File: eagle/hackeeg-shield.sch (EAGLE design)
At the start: 142 parts, among them IC1 ADS1299IPAG, IC10 TXB0108PWR, IC11 TXB0108PWR, IC2 TPS72325DBVT, IC3 TPS73225DBVT, IC5 24AA256UID, IC6 TPS60403DBVT, IC7 OPA376DBV, IC8 OPA376DBV, IC9 TXS0102DCUR

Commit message: Modified version that uses isolated SPI and isolated DC-DC converter (not tested much!)
To enable use of the EMG shield while the Arduino is galvanically connected to mains (in our scenario since it also containers motor driver controllers).

Basic communication works, but signal quality is not tested yet.

Issues:
- Spikes in signals, probably SPI issues
- MCU led polarity is wrong
- AIMTEC isolator doesn't fit well (keep out area is on the wrong side)
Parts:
- removed C43, C45, C47, C49: 4.7nF, SparkFun-Passives:CAP0603-CAP
- removed C51, C52, C54, C56, C58, C61, C70, C72: 1uF, SparkFun-Passives:CAP0603-CAP
- removed C53, C55, C57, C59, C71, C73: 0.1uF, SparkFun-Passives:CAP0603-CAP
- removed C66: 0.01uF, SparkFun-Passives:CAP0603-CAP
- removed IC10, IC11: TXB0108PWR, adafruit:TXB0108PWR
- removed IC2: TPS72325DBVT, TPS723xx:TPS732XXDBV
- removed IC3: TPS73225DBVT, TPS32xx:TPS732XXDBV
- removed IC5: 24AA256UID, microchip:24LC256SN
- removed IC6: TPS60403DBVT, TPS604xx:TPS604XXDBV
- removed IC9: TXS0102DCUR, adafruit:TXS0102
- removed JP1: CONFIG1, headers:PINHD-2X12
- removed JP15: External Sync, SparkFun-Connectors:M04JST-PTH
- removed JP16: Electrodes, OS302-R241:302-R241
- removed JP2: CONFIG0, headers:PINHD-2X10
- removed JP23: XIO, SmartPrj:PINHD-2X18
- removed JP3: BOARD_ADDRESS, headers:PINHD-2X4
- removed JP4: 5V-2.5V, headers:PINHD-1X3
- removed JP5: -2.5V-GND, headers:PINHD-1X3
- removed JP6: SRB1-BIAS, adafruit:PINHD-1X3
- removed JP7: SRB2-REF_ELEC, adafruit:PINHD-1X3
- removed JP8: SRB1-REF_ELEC, adafruit:PINHD-1X3
- removed JP9: BIASOUT_BIASIN_BIAS_ELEC, headers:PINHD-1X3
- removed R19, R20, R21: 10k, SparkFun-Passives:RESISTOR0603-RES
- removed R24: 4.99k, SparkFun-Passives:RESISTOR0603-RES
- removed SPI: SPI, SmartPrj:PINHD-2X3
- removed TP2: AVSS_TEST_POINT, adafruit:PINHD-1X1
- added C67, C69: 0.1uF, SparkFun-Passives:CAP0603-CAP
- added D3, D4: BLUE, SparkFun-LED:LED-WHITE
- added ESD1, ESD2, ESD3, ESD4, ESD5, ESD6, ESD7, ESD8: ESD7L, ESD7L:ESD7L
- added ISO1: AM1DM-0505SH60-NZ, Aimtec AM1D:AM1DM-0505SH60-NZ
- added J1, J10, J11: 533981071, Molex Picoblade 53398-1071:533981071
- added J2, J3, J4, J5, J6, J7, J8, J9: SJ1-3535N, SJ1-3535N-a:SJ1-3535N
- added R10, R11: 4.99k, SparkFun-Passives:RESISTOR0603-RES
- added R12, R13, R14, R15, R16, R17: 0R, SparkFun-Passives:RESISTOR0603-RES
- added R5, R8: 270, SparkFun-Passives:RESISTOR0603-RES
- added R7: 1k, SparkFun-Passives:RESISTOR0603-RES
- added R9: 10k, SparkFun-Passives:RESISTOR0603-RES
- added SJ4: CLK_SEL, jumper:SJ2W
- added SW1: SPST_TACT-EVQQ2, adafruit:SPST_TACT-EVQQ2
- added U1: R1SE-0505-R, R1SE-0505-R:R1SE-0505-R
- added U2: MAX14483AAP+, MAX14483AAP:MAX14483AAP+
- added U3, U4: ADP151AUJZ-3.3, ADP151AUJZ-3.3:ADP151AUJZ-3.3
- C1, C28: value 2.2uF -> 10uF
- C2: value 10 uF -> 4.7uF
- C26: value 1uF -> 10pF
- C29, C30: value 1uF -> 100nF
- C3: value 10uF -> 4.7uF
- C31: value 0.01uF -> 10pF
- C32: value 1uF -> 100pF
- C34, C36, C38, C40, C42, C44, C46, C48, C62: value 4.7nF -> NC
- C35: value 4.7nF -> 1 pF TVS
- C37: value 4.7nF -> 220pF
- C39, C41: value 4.7nF -> 100nF
- C4: value 2.2uF -> 1uF
- D1: value RED -> GREEN
- D2: value BLUE -> ORANGE
- L1: value 3.3 uH -> 6.8μH; device SparkFun-Passives:INDUCTOR0805 -> SparkFun-Coils:1.0μH-0805_WIDE-1.0μH-1.4A-0.07OHM-1.4MM_H; SPICEPREFIX (none) -> L
- L2, L3, L4: value 3.3 uH -> 3.3μH; device SparkFun-Passives:INDUCTOR0805 -> SparkFun-Coils:1.0μH-0805_WIDE-1.0μH-1.4A-0.07OHM-1.4MM_H
- R6: value 3.98K -> 4.99k
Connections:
- removed net !ADC_CS_0: JP2.10, JP21.4
- removed net !ADC_CS_1: JP2.12, JP20.8
- removed net !ADC_CS_2: JP2.14, JP23.33
- removed net !ADC_CS_3: JP2.16, JP23.4
- removed net !ADC_PWDN_0: JP1.22, JP23.13
- removed net !ADC_PWDN_1: JP1.24, JP23.14
- removed net !ADC_RESET_0: JP1.18, JP23.27
- removed net !ADC_RESET_1: JP1.20, JP23.28
- removed net !ADS_PWDN: IC11.B5, JP1.21, JP1.23
- removed net !ADS_RESET: IC11.B1, JP1.17, JP1.19
- removed net !ADS_SPI_CS: IC11.B6, JP2.11, JP2.13, JP2.15, JP2.9
- removed net +2.5V: C6.1, JP4.3, L2.2
- removed net -2.5V: C3.1, JP5.1, L1.2
- removed net ADC_CLK_0: JP1.10, JP25.8
- removed net ADC_CLK_1: JP1.12, JP25.5
- removed net ADC_DRDY_0: JP1.2, JP23.5
- removed net ADC_DRDY_1: JP1.4, JP23.6
- removed net ADC_DRDY_2: JP1.6, JP23.7
- removed net ADC_DRDY_3: JP1.8, JP23.8
- removed net ADC_START_0: JP1.14, JP23.11
- removed net ADC_START_1: JP1.16, JP23.12
- removed net ADS_CLK: IC10.B5, JP1.11, JP1.9
- removed net ADS_CLKSEL: IC10.B1, JP23.29
- removed net ADS_DRDY: IC10.B2, JP1.1, JP1.3, JP1.5, JP1.7
- removed net ADS_SPI_CLK: IC10.B4, JP15.3, JP2.5, JP2.7
- removed net ADS_SPI_IN: IC10.B6, JP2.17, JP2.19
- removed net ADS_SPI_OUT: IC10.B3, JP2.1, JP2.3
- removed net ADS_START: IC11.B2, JP1.13, JP1.15, JP15.2
- removed net ARD_SCL: IC9.B2, JP22.8
- removed net ARD_SDA: IC9.B1, JP22.7
- removed net AVSS: C11.2, C12.2, C17.2, C18.2, C19.2, C20.2, C21.2, C22.2, C23.2, C29.2, C30.2, C33.2, C51.2, C61.2, C7.2, C8.2, IC1.AVSS1, IC1.AVSS@1, IC1.AVSS@2, IC1.AVSS@3, IC1.AVSS@4, IC1.AVSS@5, IC1.VREFN, IC7.V_N, IC8.V_N, JP5.2, R22.2, TP2.1
- removed net BIASIN: IC1.BIASIN, JP9.3
- removed net BIASOUT: C66.1, IC1.BIASOUT, JP9.2, R6.2
- removed net BIAS_ELEC: JP6.1, JP9.1, R24.2
- removed net BIAS_ELEC_CON: JP16.24, R24.1
- removed net IOREF: C54.2, C55.2, C58.2, C59.2, C72.2, C73.2, IC10.VCCB, IC11.VCCB, IC9.VCCB, JP26.2
- removed net N$101: JP23.15
- removed net N$102: JP23.17
- removed net N$103: JP23.19
- removed net N$104: JP23.21
- removed net N$107: JP23.23
- removed net N$108: JP23.25
- removed net N$111: JP23.31
- removed net N$24: JP21.7
- removed net N$27: JP20.3
- removed net N$28: JP20.4
- removed net N$29: JP20.5
- removed net N$30: JP20.6
- removed net N$31: JP20.7
- removed net N$33: JP20.10
- removed net N$34: JP21.1
- removed net N$35: JP21.2
- removed net N$36: JP21.3
- removed net N$37: IC9.OE, R4.2
- removed net N$38: JP21.5
- removed net N$39: JP21.6
- removed net N$40: JP21.8
- removed net N$41: JP22.1
- removed net N$42: JP22.2
- removed net N$45: JP22.5
- removed net N$46: JP22.6
- removed net N$48: JP24.8
- removed net N$49: JP24.7
- removed net N$50: JP24.6
- removed net N$501: JP25.7
- removed net N$51: JP24.5
- removed net N$510: JP25.6
- removed net N$52: JP24.4
- removed net N$53: JP24.3
- removed net N$561: IC10.OE, R2.2
- removed net N$562: IC11.OE, R3.2
- removed net N$570: JP26.5
- removed net N$571: JP23.1
- removed net N$572: JP23.2
- removed net N$59: JP25.4
- removed net N$60: JP25.3
- removed net N$6001: JP20.2
- removed net N$6002: JP20.1
- removed net N$61: JP25.2
- removed net N$62: JP26.8
- removed net N$63: JP26.7
- removed net N$64: JP26.6
- removed net N$67: JP26.3
- removed net N$78: JP23.34
- removed net N$79: JP23.32
- removed net N$80: JP23.30
- removed net N$82: JP23.26
- removed net N$83: JP23.24
- removed net N$84: JP23.22
- removed net N$85: JP23.20
- removed net N$86: JP23.18
- removed net N$87: JP23.16
- removed net N$90: JP23.10
- removed net N$95: JP23.3
- removed net N$98: JP23.9
- removed net RESET: SPI.5
- removed net SCL: IC5.SCL, IC9.A2
- removed net SDA: IC5.SDA, IC9.A1
- removed net SPI0_MISO: JP2.2, SPI.1
- removed net SPI0_MOSI: JP2.18, SPI.4
- removed net SPI0_SCK: JP2.8, SPI.3
- removed net USART1_MISO: JP2.4, JP22.4
- removed net USART1_MOSI: JP2.20, JP22.3
- removed net USART1_SCK: JP2.6, JP25.1
- removed net VCC_-5V: C24.1, C28.1, IC2.EN, IC2.IN, L3.2
- new net DRDY_D69: JP24.1, R17.1
- new net N$12: R17.2, U2.!OFAULT
- new net N$22: R15.2, U2.IAUX
- new net N$23: R16.2, U2.OSDO
- new net N$44: R7.2, U2.!SDOEN
- new net PE: C2.2, C3.2, C67.2, ISO1.VIN-, JP26.6, JP26.7, R7.1, R8.1, U1.-VIN, U2.GNDB
- new net PGND: C26.1, C31.1, C32.2, IC1.BIASIN, J10.10, J2.1, R10.2, R11.2
- new net SPI2_CS: JP20.2, R12.1
- new net SPI2_MISO: JP25.5, R16.1
- new net SPI2_MOSI: JP25.3, R14.1
- new net SPI2_SCK: JP22.7, R13.1
- new net START_D68: JP24.2, R15.1
- new net VCC_MCU: C2.1, C67.1, JP26.5, L1.1, U2.VDDB
- net !PWDN: now also C41.1, R4.1, SW1.P, SW1.P1; no longer IC11.A5
- net !RESET: now also C39.1, R9.1; no longer IC11.A1
- net !SPI_CS: now also J1.4, R2.2, U2.!OCS; no longer IC11.A6
- net AGND: now also C11.2, C12.2, C17.2, C18.2, C19.2, C20.2, C21.2, C22.2, C23.2, C29.2, C32.1, C33.2, C35.2, C69.2, C7.2, C8.2, D3.C, ESD1.P$3, ESD2.P$3, ESD3.P$3, ESD4.P$3, ESD5.P$3, ESD6.P$3, ESD7.P$3, ESD8.P$3, IC1.AVSS1, IC1.AVSS@1, IC1.AVSS@2, IC1.AVSS@3, IC1.AVSS@4, IC1.AVSS@5, IC1.VREFN, IC7.V_N, IC8.V_N, ISO1.VOUT-, J1.1, J1.11, J1.12, J10.11, J10.12, J11.11, J11.12, R22.2, SJ4.3, SW1.S, SW1.S1, U1.-VOUT, U2.!IRDY, U2.GNDA, U3.GND, U4.GND; no longer C2.2, C29.1, C3.2, C31.2, C32.2, C34.2, C35.1, C36.2, C37.1, C38.2, C39.1, C40.2, C41.1, C42.2, C43.1, C44.2, C45.1, C46.2, C47.1, C48.2, C49.1, C51.1, C52.1, C53.1, C54.1, C55.1, C56.1, C57.1, C58.1, C59.1, C61.1, C70.1, C71.1, C72.1, C73.1, IC10.A7, IC10.A8, IC10.B7, IC10.B8, IC10.GND, IC11.A3, IC11.A4, IC11.A7, IC11.A8, IC11.B3, IC11.B4, IC11.B7, IC11.B8, IC11.GND, IC2.GND, IC3.GND, IC5.GND, IC5.WP, IC6.GND, IC9.GND, JP15.4, JP16.4, JP16.5, JP16.6, JP23.35, JP23.36, JP5.3, R19.1, R20.1, R21.1, SPI.6
- net AIN1N: now also C34.2; no longer C35.2
- net AIN2N: now also C36.2; no longer C37.2
- net AIN3N: now also C38.2; no longer C39.2
- net AIN4N: now also C40.2; no longer C41.2
- net AIN5N: now also C42.2; no longer C43.2
- net AIN6N: now also C44.2; no longer C45.2
- net AIN7N: now also C46.2; no longer C47.2
- net AIN8N: now also C48.2; no longer C49.2
- net AVDD: now also C29.1, C30.2, C6.1, L2.2; no longer JP16.2, JP4.2
- net BIASINV: now also R6.2; no longer C66.2, JP15.1, JP16.3, R6.1
- net BOARD_ADDR_0: no longer IC5.A0, JP3.3, R19.2
- net BOARD_ADDR_1: no longer IC5.A1, JP3.1, R20.2
- net BOARD_ADDR_2: no longer IC5.A2, R21.2
- net CLK: now also J1.3; no longer IC10.A5
- net CLKSEL: now also R3.1; no longer IC10.A1
- net DRDY: now also J1.9, U2.!IFAULT; no longer IC10.A2
- net DVDD: now also C24.1, C39.2, C41.2, C69.1, L3.2, R4.2, R9.2, SJ4.1, U2.VDDA; no longer C52.2, C53.2, C56.2, C57.2, C70.2, C71.2, IC10.VCCA, IC11.VCCA, IC5.VCC, IC9.VCCA, JP16.1, JP26.4, JP3.2, JP3.4, R3.1, R4.1
- net IN1N: now also ESD1.P$2, J10.7, J2.3; no longer JP16.8
- net IN1P: now also ESD1.P$1, J10.8, J2.2; no longer JP16.7
- net IN2N: now also ESD2.P$2, J10.5, J3.3; no longer JP16.10
- net IN2P: now also ESD2.P$1, J10.6, J3.2; no longer JP16.9
- net IN3N: now also ESD3.P$2, J10.3, J4.3; no longer JP16.12
- net IN3P: now also ESD3.P$1, J10.4, J4.2; no longer JP16.11
- net IN4N: now also ESD4.P$2, J10.1, J5.3; no longer JP16.14
- net IN4P: now also ESD4.P$1, J10.2, J5.2; no longer JP16.13
- net IN5N: now also ESD5.P$2, J11.9, J6.3; no longer JP16.16
- net IN5P: now also ESD5.P$1, J11.10, J6.2; no longer JP16.15
- net IN6N: now also ESD6.P$2, J11.7, J7.3; no longer JP16.18
- net IN6P: now also ESD6.P$1, J11.8, J7.2; no longer JP16.17
- net IN7N: now also ESD7.P$2, J11.5, J8.3; no longer JP16.20
- net IN7P: now also ESD7.P$1, J11.6, J8.2; no longer JP16.19
- net IN8N: now also ESD8.P$2, J11.3, J9.3; no longer JP16.22
- net IN8P: now also ESD8.P$1, J11.4, J9.2; no longer JP16.21
- net N$1: now also U4.VOUT; no longer IC3.OUT
- net N$10: now also J11.1, R6.1; no longer C26.1, IC6.CFLY_N
- net N$11: now also R5.1, U2.SBA; no longer C32.1, IC3.NR/FB
- net N$13: now also D4.C, U2.SAA; no longer C31.1, IC2.NR/FB
- net N$16: now also R12.2, U2.!ICS; no longer IC8.P_IN, JP7.2
- net N$17: now also R13.2, U2.ISCLK; no longer IC8.N_IN, IC8.OUT, JP8.3
- net N$18: now also C31.2, C37.1, R10.1; no longer IC7.N_IN, JP6.3
- net N$2: now also C15.1, C16.1, L3.1, U3.VOUT; no longer C1.1, C2.1, IC2.OUT, L1.1
- net N$20: now also R3.2, SJ4.2; no longer JP24.1
- net N$21: now also R14.2, U2.ISDI; no longer JP26.1
- net N$54: now also C26.2, C37.2, IC7.N_IN, R11.1; no longer JP24.2
- net N$6: now also C3.1, ISO1.VIN+, L1.2, U1.+VIN; no longer JP20.9
- net N$7: now also D4.A, R8.2; no longer C15.1, C16.1, IC6.OUT, L3.1
- net N$9: now also D3.A, R5.2; no longer C26.2, IC6.CFLY_P
- net REF_ELEC: now also IC8.P_IN; no longer JP7.1, JP8.1
- net REF_ELEC_CON: now also C35.1, J10.9, J3.1; no longer JP16.23
- net SPI_CLK: now also J1.5, U2.OSCLK; no longer IC10.A4
- net SPI_IN: now also J1.6, U2.OSDI; no longer IC10.A6
- net SPI_OUT: now also J1.8, U2.ISDO; no longer IC10.A3
- net SRB1: now also IC1.SRB1, IC8.N_IN, IC8.OUT; no longer IC1.SRB2, JP6.2, JP8.2
- net SRB2: now also IC1.SRB2, J1.10; no longer IC1.SRB1, JP7.3
- net START: now also J1.7, U2.OAUX; no longer IC11.A2
- net VCC_5V: now also C28.1, ISO1.VOUT+, J1.2, U1.+VOUT; no longer SPI.2
- net VCC_5V_FILTERED: now also C1.1, U3.EN, U3.VIN, U4.EN, U4.VIN; no longer IC3.EN, IC3.IN, IC6.IN, JP4.1
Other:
- note added: "- SPI2_MOSI: PC_3, A2 - SPI2_MISO: PC_2, A4 - SPI2_CS: PB_9, D14 - SPI2_SCK: PB_10, D36 - D68 - D69"
- note added: "11 and 12 are the supports, and can be connected to AGND, not to a signal"
- note added: "Adapted by Frodo Muijzer, University of Twente 2022"
- note added: "Bias driver, provides half of supply voltage as Patient Ground"
- note added: "CLK_SEL high = use internal clock"
- note added: "Depending on the ADS type, 4, 6 or 8 jacks will be populated"
- note added: "Do the unused channels need to be shorted to AGND?"
- note added: "Don't fully understand from the datasheet whether or not the !SDOEN has to be pulled low seperate from the CS line to activate the OSDO."
- note added: "Either the jacks, or J10/J11 are placed"
- note added: "First input in green casing to indicate PGND"
- note added: "ISO Active LED"
- note added: "Molex picoblade"
- note added: "Only one of the two isolated DCDC converters is required"
- note added: "R10+R11 maintain safety while reducing output impedance of bias driver. Watch out for instability."
- note added: "Red = tip White = ring Black = sleeve"
- note added: "Ref Electrode buffer, connected to SRB1, can be used for common reference mode."
- note added: "Remaining inputs in black SJ1-3535NG"
- note added: "SPI_CS pull-up needed?"
- note added: "Second input in Blue Casing to indicate REF"
- note removed: "(2 no-connect positions for jumper storage)"
- note removed: "(This side to electrode connector)"
- note removed: "22"
- note removed: "23"
- note removed: "24"
- note removed: "25"
- note removed: "26"
- note removed: "27"
- note removed: "28"
- note removed: "29"
- note removed: "30"
- note removed: "31"
- note removed: "32"
- note removed: "33"
- note removed: "34"
- note removed: "35"
- note removed: "36"
- note removed: "37"
- note removed: "38"
- note removed: "39"
- note removed: "40"
- note removed: "41"
- note removed: "42"
- note removed: "43"
- note removed: "44"
- note removed: "45"
- note removed: "46"
- note removed: "47"
- note removed: "48"
- note removed: "49"
- note removed: "50"
- note removed: "51"
- note removed: "52"
- note removed: "53"
- note removed: "ADS1299 Level Shifting"
- note removed: "Bias"
- note removed: "Configuration jumpers"
- note removed: "I2C EEPROM Level Shifting"
- note removed: "Pins not labeled are not connected (NC)"
- note removed: "Settings I2C EEPROM with UID"
- note removed: "Stimulus-Response Buffer (SRB)"

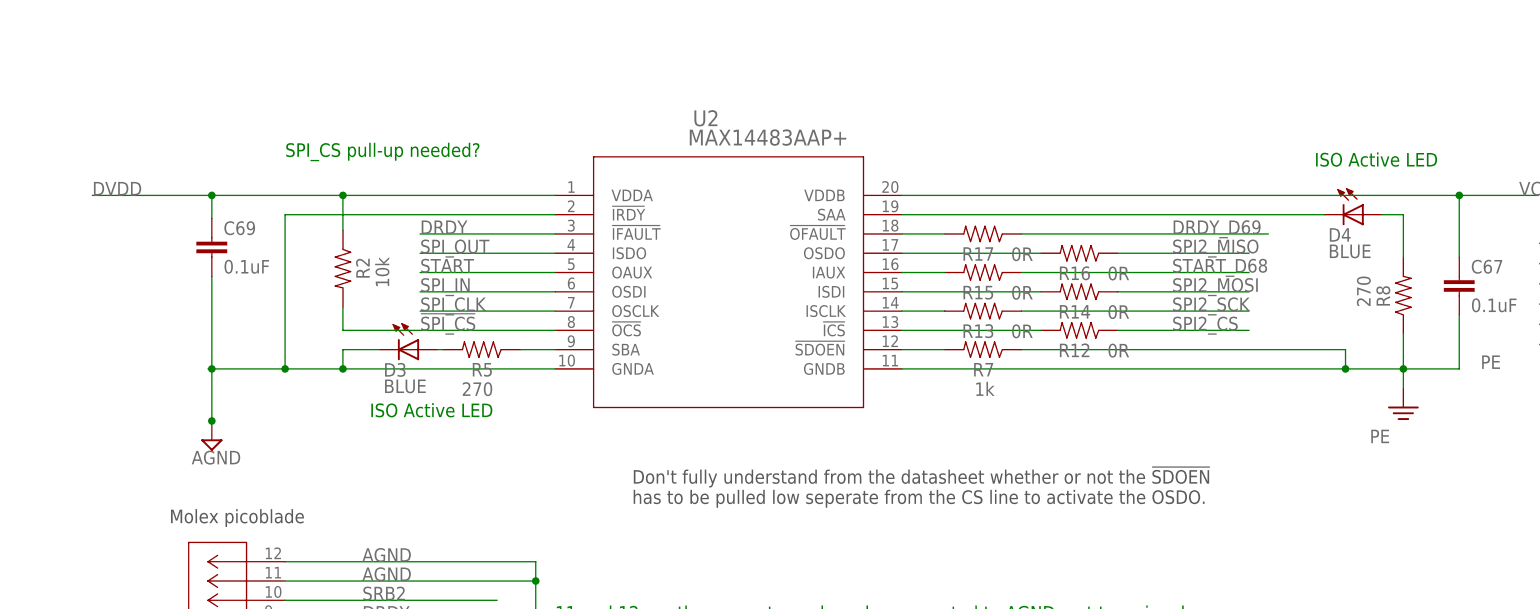
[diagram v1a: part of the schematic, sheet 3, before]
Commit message: Patched led, removed header ch1 to 4, added drdy pull up
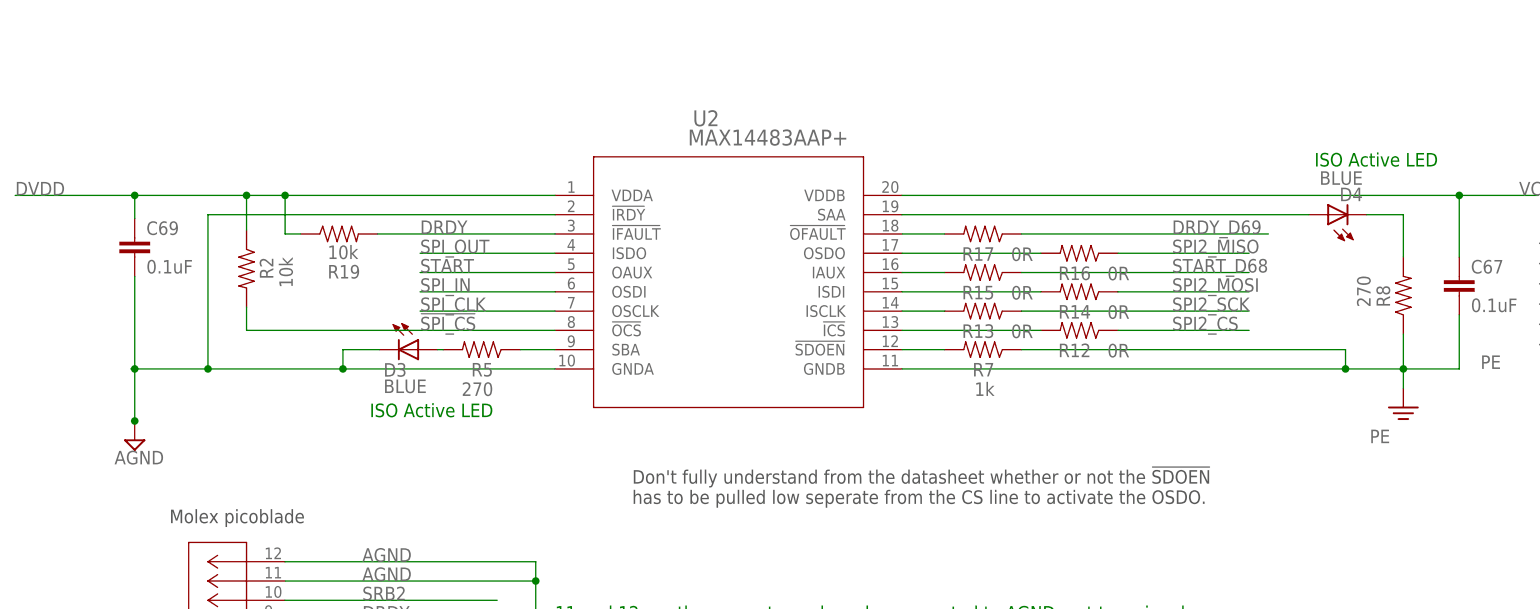
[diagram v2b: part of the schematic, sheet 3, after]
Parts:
- removed J10: 533981071, Molex Picoblade 53398-1071:533981071
- added R19: 10k, SparkFun-Passives:RESISTOR0603-RES
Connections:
- net AGND: no longer J10.11, J10.12
- net DRDY: now also R19.2
- net DVDD: now also R19.1
- net IN1N: no longer J10.7
- net IN1P: no longer J10.8
- net IN2N: no longer J10.5
- net IN2P: no longer J10.6
- net IN3N: no longer J10.3
- net IN3P: no longer J10.4
- net IN4N: no longer J10.1
- net IN4P: no longer J10.2
- net N$13: now also R8.2; no longer U2.SAA
- net N$7: now also U2.SAA; no longer R8.2
- net PGND: no longer J10.10
- net REF_ELEC_CON: no longer J10.9
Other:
- note removed: "SPI_CS pull-up needed?"
- moved on the sheet: C69, D4, R2

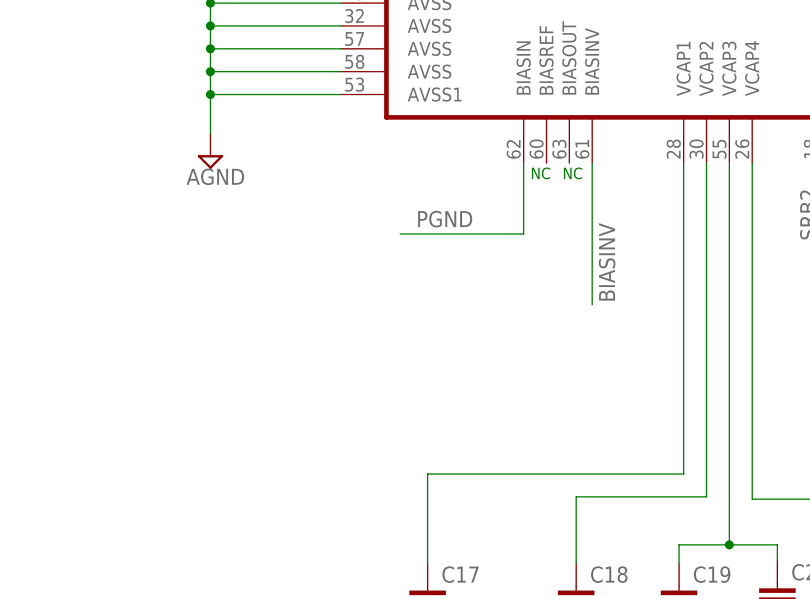
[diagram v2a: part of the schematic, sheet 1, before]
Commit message: added NC res/cap to potentially use the RLD
Added C and R between 61 and 63 and moved R6 closer to chip, to enable testing with RLD and future patch to enable it.
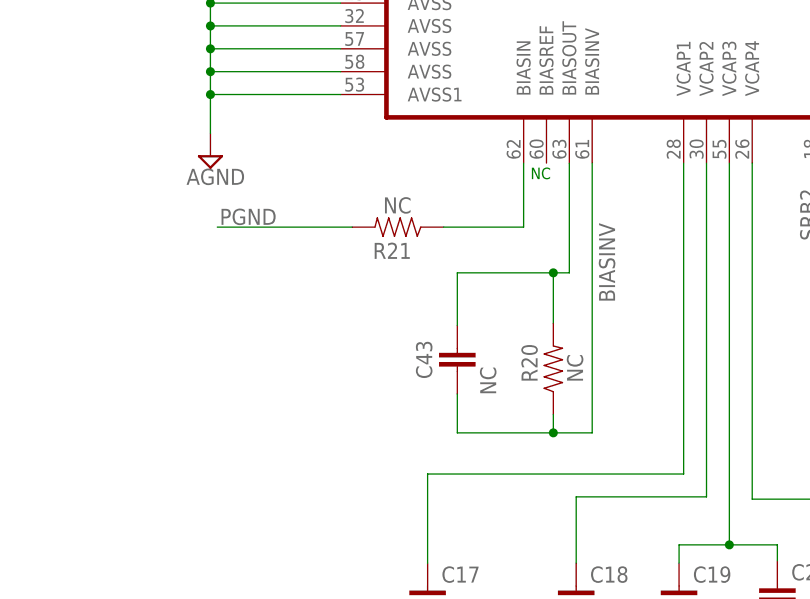
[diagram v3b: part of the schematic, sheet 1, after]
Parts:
- added C43: NC, SparkFun-Passives:CAP0603-CAP
- added R20, R21: NC, SparkFun-Passives:RESISTOR0603-RES
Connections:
- new net N$24: C43.1, IC1.BIASOUT, R20.2
- new net N$25: IC1.BIASIN, R21.1
- net BIASINV: now also C43.2, R20.1
- net PGND: now also R21.2; no longer IC1.BIASIN
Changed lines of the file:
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@@
 <part name="J9" library="SJ1-3535N-a" deviceset="SJ1-3535N" device=""/>
 <part name="R19" library="SparkFun-Passives" deviceset="RESISTOR" device="0603-RES" value="10k"/>
+<part name="R20" library="SparkFun-Passives" deviceset="RESISTOR" device="0603-RES" value="NC"/>
+<part name="C43" library="SparkFun-Passives" deviceset="CAP" device="0603-CAP" value="NC"/>
+<part name="R21" library="SparkFun-Passives" deviceset="RESISTOR" device="0603-RES" value="NC"/>
 </parts>
 <sheets>
@@
 <text x="271.78" y="142.494" size="1.27" layer="91">NC</text>
 <text x="378.46" y="198.12" size="1.778" layer="97">CLK_SEL high = use internal clock</text>
-<text x="275.336" y="142.494" size="1.27" layer="91">NC</text>
 </plain>
 <instances>
@@
 <attribute name="NAME" x="372.491" y="60.96" size="1.778" layer="95" rot="MR0"/>
 <attribute name="VALUE" x="374.269" y="68.072" size="1.778" layer="96" rot="MR0"/>
+</instance>
+<instance part="R20" gate="G$1" x="274.32" y="121.412" smashed="yes" rot="R90">
+<attribute name="NAME" x="272.5674" y="119.888" size="1.778" layer="95" rot="R90"/>
+<attribute name="VALUE" x="277.622" y="119.888" size="1.778" layer="96" rot="R90"/>
+</instance>
+<instance part="C43" gate="G$1" x="263.652" y="121.158" smashed="yes" rot="MR0">
+<attribute name="NAME" x="259.08" y="120.269" size="1.778" layer="95" rot="MR90"/>
+<attribute name="VALUE" x="266.192" y="118.491" size="1.778" layer="96" rot="MR90"/>
+</instance>
+<instance part="R21" gate="G$1" x="257.048" y="137.16" smashed="yes" rot="R180">
+<attribute name="NAME" x="258.572" y="135.4074" size="1.778" layer="95" rot="R180"/>
+<attribute name="VALUE" x="258.572" y="140.462" size="1.778" layer="96" rot="R180"/>
 </instance>
 </instances>
@@
 <segment>
 <pinref part="IC1" gate="G$1" pin="BIASINV"/>
-<wire x1="278.638" y1="144.272" x2="278.638" y2="128.524" width="0.1524" layer="91"/>
+<wire x1="278.638" y1="144.272" x2="278.638" y2="114.3" width="0.1524" layer="91"/>
 <label x="281.178" y="128.778" size="1.778" layer="95" rot="R90"/>
+<pinref part="R20" gate="G$1" pin="1"/>
+<wire x1="274.32" y1="116.332" x2="274.32" y2="114.3" width="0.1524" layer="91"/>
+<wire x1="278.638" y1="114.3" x2="274.32" y2="114.3" width="0.1524" layer="91"/>
+<pinref part="C43" gate="G$1" pin="2"/>
+<wire x1="274.32" y1="114.3" x2="263.652" y2="114.3" width="0.1524" layer="91"/>
+<wire x1="263.652" y1="114.3" x2="263.652" y2="118.618" width="0.1524" layer="91"/>
+<junction x="274.32" y="114.3"/>
 </segment>
 </net>
@@
 <net name="PGND" class="0">
 <segment>
-<wire x1="271.018" y1="144.272" x2="271.018" y2="136.398" width="0.1524" layer="91"/>
-<pinref part="IC1" gate="G$1" pin="BIASIN"/>
-<wire x1="271.018" y1="136.398" x2="257.302" y2="136.398" width="0.1524" layer="91"/>
-<label x="259.08" y="137.16" size="1.778" layer="95"/>
+<wire x1="251.968" y1="137.16" x2="236.982" y2="137.16" width="0.1524" layer="91"/>
+<label x="237.236" y="137.414" size="1.778" layer="95"/>
+<pinref part="R21" gate="G$1" pin="2"/>
 </segment>
 </net>
@@
 </segment>
 </net>
+<net name="N$24" class="0">
+<segment>
+<pinref part="IC1" gate="G$1" pin="BIASOUT"/>
+<wire x1="276.098" y1="144.272" x2="276.098" y2="132.08" width="0.1524" layer="91"/>
+<wire x1="276.098" y1="132.08" x2="274.32" y2="132.08" width="0.1524" layer="91"/>
+<pinref part="R20" gate="G$1" pin="2"/>
+<wire x1="274.32" y1="132.08" x2="274.32" y2="126.492" width="0.1524" layer="91"/>
+<wire x1="274.32" y1="132.08" x2="263.652" y2="132.08" width="0.1524" layer="91"/>
+<junction x="274.32" y="132.08"/>
+<pinref part="C43" gate="G$1" pin="1"/>
+<wire x1="263.652" y1="132.08" x2="263.652" y2="126.238" width="0.1524" layer="91"/>
+</segment>
+</net>
+<net name="N$25" class="0">
+<segment>
+<pinref part="R21" gate="G$1" pin="1"/>
+<wire x1="262.128" y1="137.16" x2="271.018" y2="137.16" width="0.1524" layer="91"/>
+<pinref part="IC1" gate="G$1" pin="BIASIN"/>
+<wire x1="271.018" y1="137.16" x2="271.018" y2="144.272" width="0.1524" layer="91"/>
+</segment>
+</net>
